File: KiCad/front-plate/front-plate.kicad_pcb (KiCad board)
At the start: 2 copper layers, 337.8 x 137.2 mm, 94 parts, among them SW1 keys, SW10 keys, SW11 keys, SW12 keys, SW13 keys, SW14 keys, SW15 keys, SW16 keys, SW17 keys, SW18 keys, SW19 keys, SW2 keys, SW20 keys, SW21 keys, SW22 keys, SW23 keys, SW24 keys, SW25 keys, SW26 keys, SW27 keys, SW28 keys, SW29 keys, SW3 keys, SW30 keys, SW31 keys, SW32 keys, SW33 keys, SW34 keys, SW35 keys, SW36 keys, SW37 keys, SW38 keys, SW39 keys, SW4 keys, SW40 keys, SW41 keys, SW42 keys, SW43 keys, SW44 keys, SW45 keys, SW46 keys, SW47 keys, SW48 keys, SW49 keys, SW5 keys, SW50 keys, SW51 keys, SW52 keys, SW53 keys, SW54 keys, SW55 keys, SW56 keys, SW57 keys, SW58 keys, SW59 keys, SW6 keys, SW60 keys, SW61 keys, SW62 keys, SW63 keys, SW64 keys, SW65 keys, SW66 keys, SW67 keys, SW68 keys, SW69 keys, SW7 keys, SW70 keys, SW71 keys, SW72 keys, SW73 keys, SW74 keys, SW75 keys, SW8 keys, SW9 keys

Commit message: front plate edge cuts
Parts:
- removed D1, D2: D, Diode_THT:D_DO-34_SOD68_P10.16mm_Horizontal
- removed SW74: keys, Holes:Cherry_MX_panel_cutout
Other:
- board size 337.8 x 137.2 mm -> 325.1 x 124.5 mm

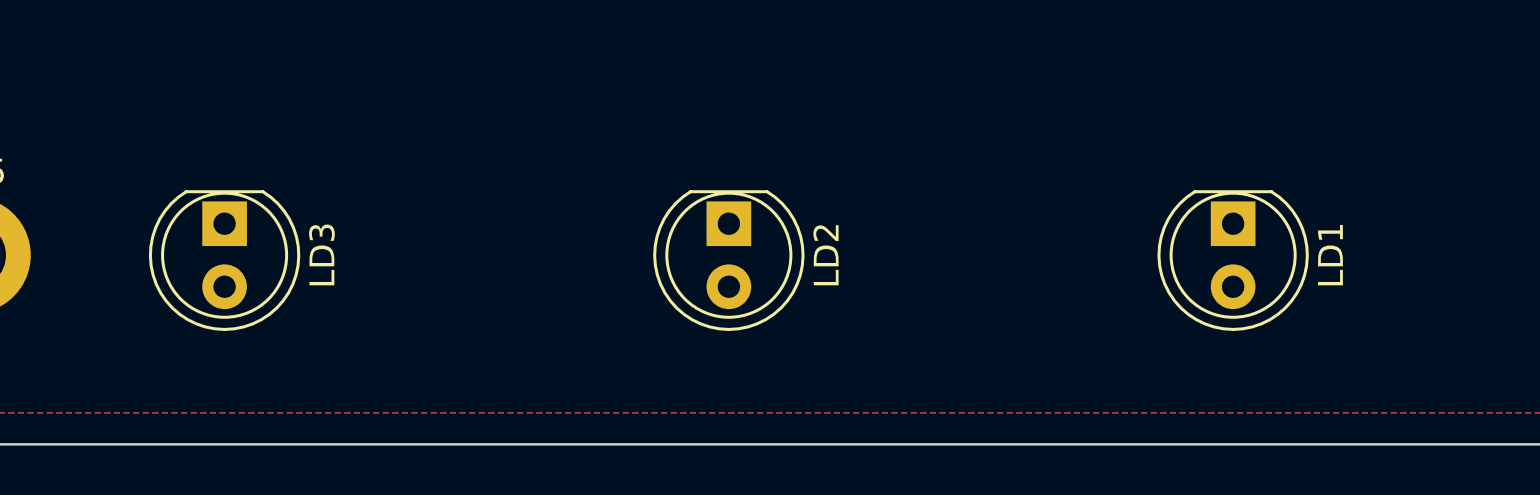
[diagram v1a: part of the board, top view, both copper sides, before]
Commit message: LED holes
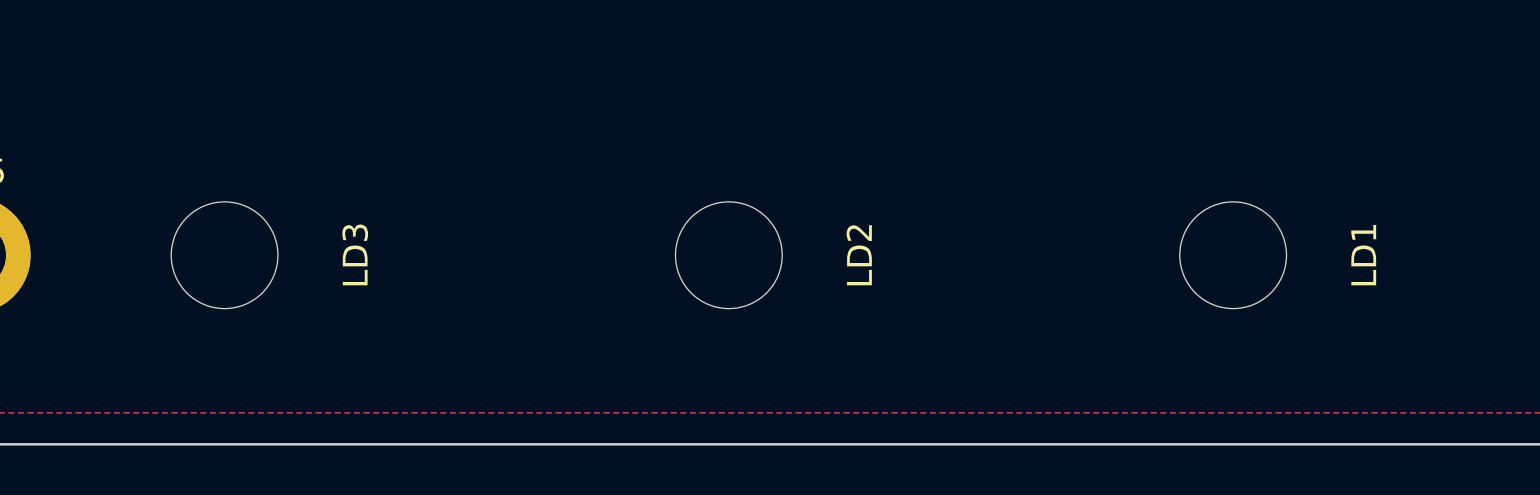
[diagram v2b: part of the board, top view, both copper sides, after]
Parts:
- LD1: value SHIFT -> MountingHole; footprint LED_THT:LED_D5.0mm -> MountingHole:MountingHole_4.3mm_M4
- LD2: value CAPS -> MountingHole; footprint LED_THT:LED_D5.0mm -> MountingHole:MountingHole_4.3mm_M4
- LD3: value CAS -> MountingHole; footprint LED_THT:LED_D5.0mm -> MountingHole:MountingHole_4.3mm_M4
- moved LD1 1.27 mm to (114.6, 224.8)
- moved LD2 1.27 mm to (94.3, 224.8)
- moved LD3 1.27 mm to (74.0, 224.8)

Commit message: stabilizer bar holes
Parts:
- removed H19: stab_return, Mounting_Keyboard_Stabilizer:Stabilizer_Cherry_MX_2.00u
- removed H20: stab_spc6.25u, Mounting_Keyboard_Stabilizer:Stabilizer_Cherry_MX_6.25u
- removed H21: stab_spc7u, Mounting_Keyboard_Stabilizer:Stabilizer_Cherry_MX_7.00u
- removed H22: stab_spc8u, Mounting_Keyboard_Stabilizer:Stabilizer_Cherry_MX_8.00u
- SW21: footprint Holes:Cherry_MX_panel_cutout -> Holes:Cherry_MX_panel_cutout_spacebar
- SW68: footprint Holes:Cherry_MX_panel_cutout -> Holes:Cherry_MX_panel_cutout_2u
- moved H10 6.48 mm to (242.9, 207.0)
- moved H11 6.48 mm to (166.7, 207.0)
